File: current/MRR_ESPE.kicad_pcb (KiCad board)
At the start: 2 copper layers, 102 x 102 mm, 166 parts, among them J1 X_MIN, J10 PART_FAN, J11 UNUSED, J12 T_BED, J13 T_E0, J14 I2C/SPI, J15 AUX1, J16 USB_B_Micro, J17 E0_FAN, J18 CASE_FAN, J19 E1_FAN, J2 Z_MIN, J20 CS_PINS, J21 X_MOTOR, J22 Z_MOTOR, J23 Y_MOTOR, J24 E0_MOTOR, J25 E1_MOTOR, J26 EXP3, J3 BED, J4 Micro_SD_Card_China, J5 Y_MIN, J6 Z_PROBE, J7 E0, J8 T_E0, J9 PWR_IN, Q1 IRLS3034PBF, Q2 IRLR8743TRPBF, Q3 WST3392, Q4 S9014, Q5 S9014, Q6 WST3392, SW1 RESET, U1 ESP32-WROOM-32D, U10 TLP182, U11 Pololu_board, U13 74HC595, U14 74HC595, U15 74HC595, U2 TPS54340DDA, U3 CH340C, U4 AMS1117-3.3, U5 Pololu_board, U6 Pololu_board, U7 74HC595, U8 Pololu_board, U9 Pololu_board

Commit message: Added v0.5
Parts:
- added C28: 100nF16V, Capacitor_SMD:C_0805_2012Metric, F.Cu at (68.6, 70.2)
- added JP30: PWR_SEL, Connector_PinHeader_2.54mm:PinHeader_1x03_P2.54mm_Vertical, F.Cu at (98.3, 74.6)
- C26, C5, C6: value 22uF10V -> 22uF6.3V
- F2: footprint projfp:Littelfuse_0456 -> projfp:Littelfuse_456
- J1, J2, J5, J6: footprint Connector_PinHeader_2.54mm:PinHeader_1x03_P2.54mm_Vertical -> Connector_JST:JST_XH_B03B-XH-A_1x03_P2.50mm_Vertical
- J17: value E0_FAN -> HS_FAN
- J19: value E1_FAN -> EXT_FAN
- J8: value T_E0 -> T_EXT
- JP21: value E0_ON -> HS_ON
- JP24: value E1_ON -> EXT_ON
- JP28: value VUSB_EN -> 5V_SEL; footprint Connector_PinHeader_2.54mm:PinHeader_1x02_P2.54mm_Vertical -> Connector_PinHeader_2.54mm:PinHeader_1x03_P2.54mm_Vertical
- U13, U14, U15, U7: footprint Package_SO:SOIC-16_3.9x9.9mm_P1.27mm -> Package_SO:TSSOP-16_4.4x5mm_P0.65mm
- moved J6 8.77 mm to (67.7, 101.8), turned to 90 degrees
- moved C21 7.07 mm to (73.8, 96.8)
- moved U13 4.71 mm to (77.8, 99.8)
- moved D15 4.55 mm to (97.8, 49.4)
- moved D14 4.51 mm to (100.2, 49.4)
- moved JP28 4.22 mm to (95.8, 53.9)
- moved R35 3.83 mm to (98.2, 79.0)
- moved J2 2.95 mm to (56.8, 101.8), turned to 90 degrees
- moved U7 2.13 mm to (69.4, 87.8)
- moved J17 2.05 mm to (137.2, 113.3)
- moved F2 1.90 mm to (118.2, 77.9)
- moved J21 1.87 mm to (51.4, 138.7)
- moved J5 1.83 mm to (50.6, 101.8), turned to 90 degrees
- moved C24 1.68 mm to (82.7, 98.2)
- moved J23 1.54 mm to (65.8, 138.7)
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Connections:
- D14 pad 1: +5V -> Net-(D14-Pad1)
- D15 pad 1: +5V -> Net-(D15-Pad1)
- D15 pad 2: Net-(D15-Pad2) -> VUSB
- J11 pad 3: Q151 -> Q152
- JP17 pad 2: Q152 -> Q151
- JP28 pad 1: Net-(D15-Pad2) -> Net-(D15-Pad1)
- JP28 pad 2: VUSB -> +5V
- R35 pad 2: TO_HEATER_BED -> Net-(JP30-Pad1)
- R38 pad 1: TO_HEATER_BED -> Net-(JP30-Pad1)
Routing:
- net SCK: track 270.9 -> 234.0 mm, vias 14 -> 13
- net Q134: track 79.2 -> 113.2 mm
- net GND: track 321.6 -> 354.0 mm, vias 155 -> 157
- net Q151: track 12.0 -> 27.8 mm, vias 0 -> 2
- net Net-(D2-Pad1): track 4.94 -> 13.8 mm, vias 0 -> 1
- net Net-(JP30-Pad3): track 7.64 -> 16.1 mm
- net Q137: track 75.7 -> 69.7 mm
- net Q138: track 49.9 -> 44.3 mm
- net Q139: track 45.6 -> 40.4 mm
- net Q152: track 19.8 -> 14.9 mm
- net 5V1: track 30.7 -> 35.7 mm
- net Net-(JP30-Pad1): track 0.00 -> 4.64 mm
- net Q140: track 86.9 -> 82.3 mm
- net Net-(U13-Pad14): track 4.78 -> 9.32 mm
- net Q141: track 62.5 -> 58.4 mm
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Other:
- board text added: "0"
- board text added: "12"
- board text added: "12V"
- board text added: "13"
- board text added: "14"
- board text added: "16"
- board text added: "17"
- board text added: "24V"
- board text added: "BEEP"
- board text added: "EN"
- board text added: "MRR ESPE v0.5"
- board text added: "VMOT"
- board text added: "Version date: 2019-10-06"
- board text added: "ZPROBE"
- board text removed: "3.3"
- board text removed: "MRR ESPE v0.4"
- board text removed: "PROBE"
- board text removed: "V"
- board text removed: "Version date: 2019-07-01"

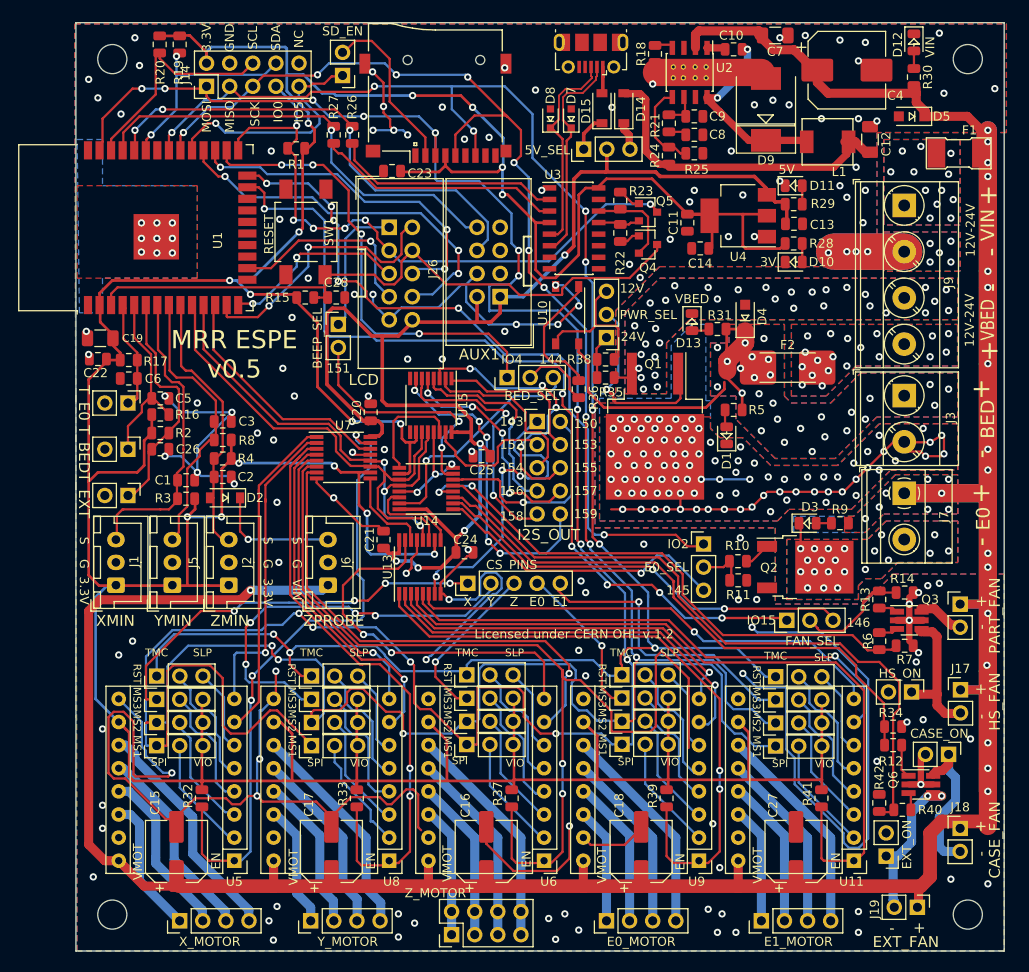
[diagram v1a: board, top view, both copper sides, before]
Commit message: Minor change to v0.5 silkscreen
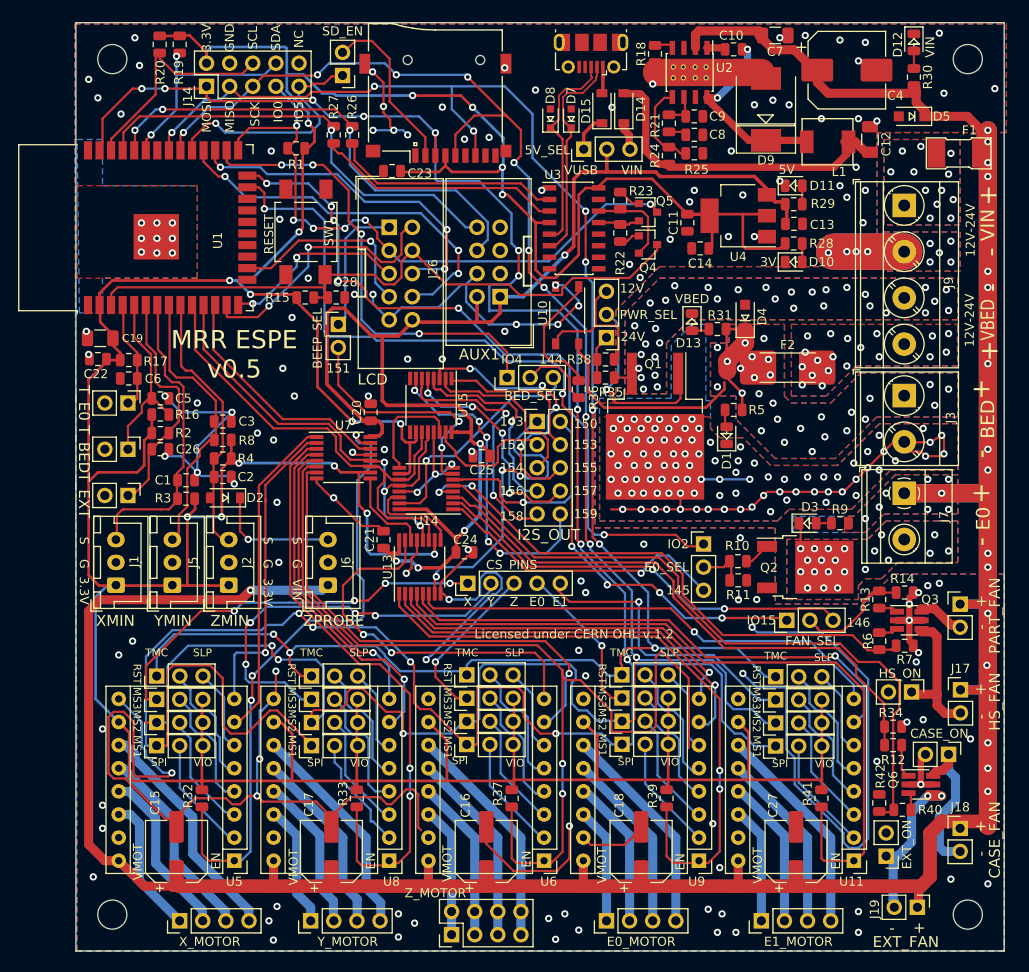
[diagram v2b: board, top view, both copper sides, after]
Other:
- board text added: "VUSB"
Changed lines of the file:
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@@
   (general
     (thickness 1.6)
-    (drawings 180)
+    (drawings 182)
     (tracks 2664)
     (zones 0)
@@
     (tags resistor)
     (attr smd)
-    (fp_text reference R12 (at 0.254 -1.778 180) (layer F.SilkS)
+    (fp_text reference R12 (at -0.006 -1.62 180) (layer F.SilkS)
       (effects (font (size 1 1) (thickness 0.15)))
     )
@@
     (tags capacitor)
     (attr smd)
-    (fp_text reference C22 (at 0.254 -1.524 180) (layer F.SilkS)
+    (fp_text reference C22 (at 0.218 -1.638 180) (layer F.SilkS)
       (effects (font (size 1 1) (thickness 0.15)))
     )
@@
     (tags resistor)
     (attr smd)
-    (fp_text reference R42 (at -2.794 0 270) (layer F.SilkS)
+    (fp_text reference R42 (at -2.93 -0.13 270) (layer F.SilkS)
       (effects (font (size 1 1) (thickness 0.15)))
     )
@@
     (descr "Through hole straight pin header, 2x05, 2.54mm pitch, double rows")
     (tags "Through hole pin header THT 2x05 2.54mm double row")
-    (fp_text reference J14 (at 1.27 -2.33 90) (layer F.SilkS)
+    (fp_text reference J14 (at -1.11 -2.056 90) (layer F.SilkS)
       (effects (font (size 1 1) (thickness 0.15)))
     )
@@
     (tags capacitor)
     (attr smd)
-    (fp_text reference C28 (at 0 -1.65) (layer F.SilkS)
+    (fp_text reference C28 (at 1 -1.7) (layer F.SilkS)
       (effects (font (size 1 1) (thickness 0.15)))
     )
@@
     )
   )
+  (gr_text VIN (at 101.1 56.2) (layer F.SilkS)
+    (effects (font (size 1 1) (thickness 0.2)))
+  )
+  (gr_text VUSB (at 95.5 56.2) (layer F.SilkS)
+    (effects (font (size 1 1) (thickness 0.2)))
+  )
   (gr_text VMOT (at 114.9 132.6 90) (layer F.SilkS)
     (effects (font (size 1 1) (thickness 0.25)))
@@
     (effects (font (size 0.85 0.85) (thickness 0.2)))
   )
-  (gr_text LCD (at 71.628 79.248) (layer F.SilkS)
+  (gr_text LCD (at 72.6 79.2) (layer F.SilkS)
     (effects (font (size 1.2 1.2) (thickness 0.3)))
   )
